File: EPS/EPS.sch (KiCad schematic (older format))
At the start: 2 parts, among them J6 CAN

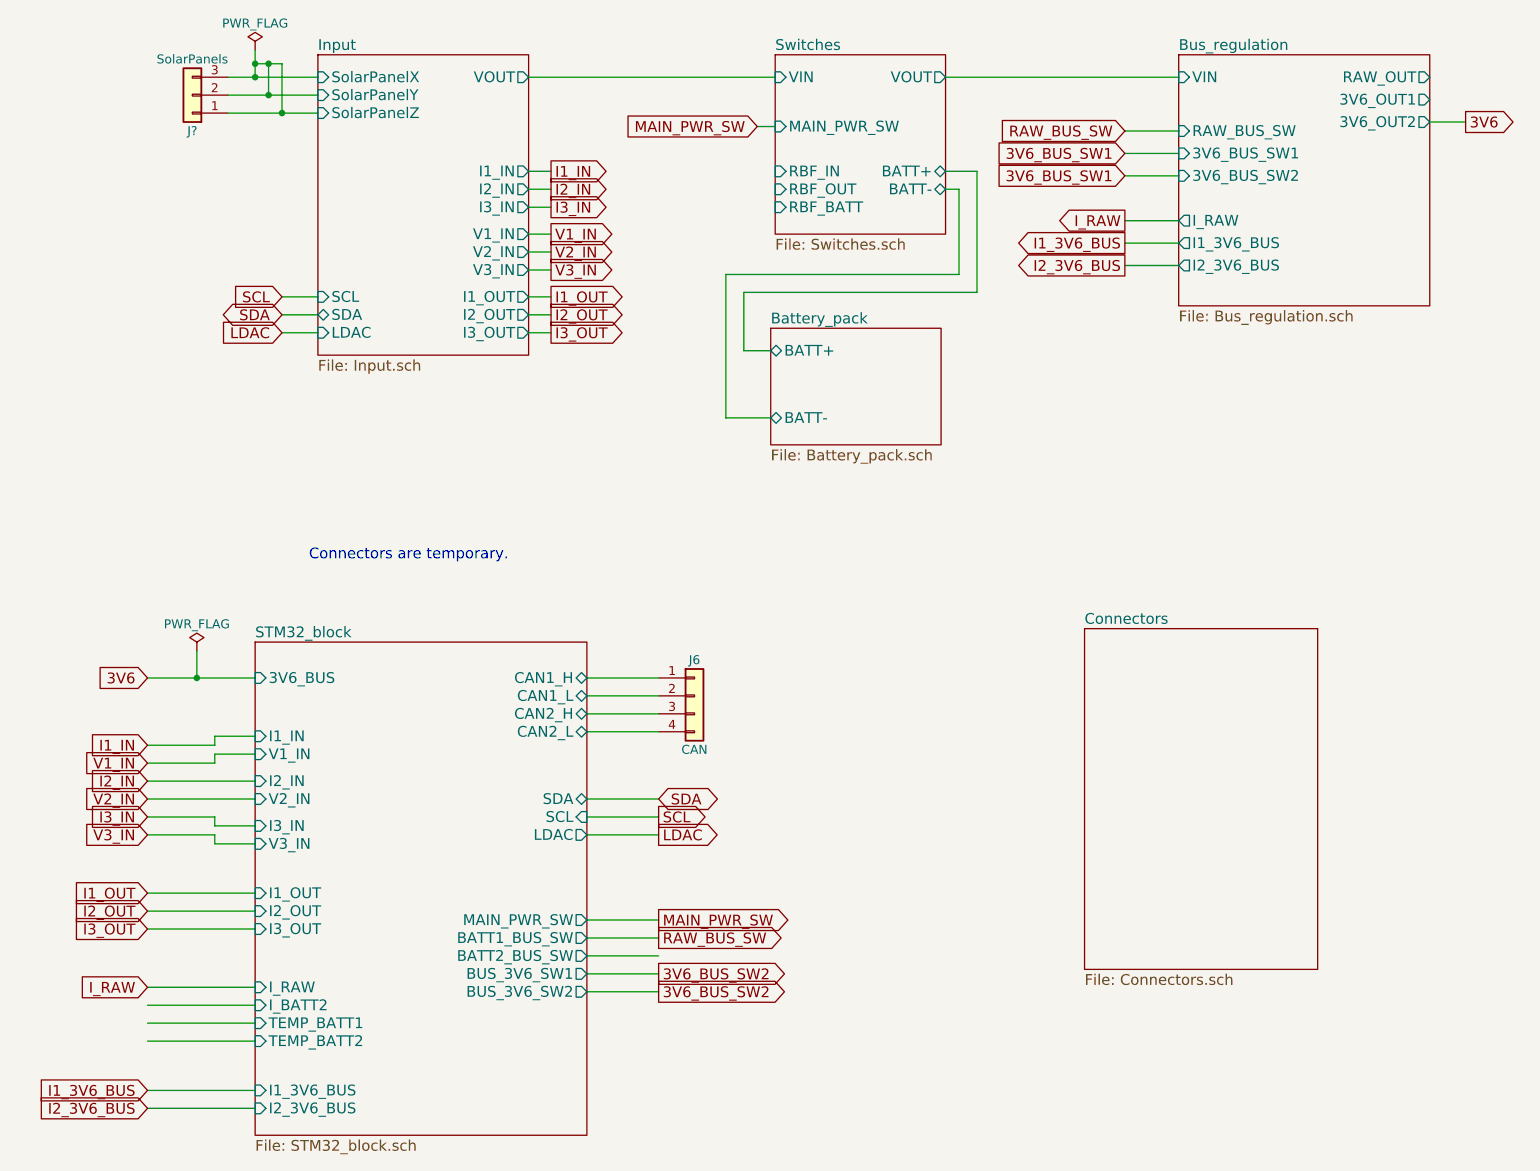
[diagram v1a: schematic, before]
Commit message: Updated Schematics
Added:
- digital pot
- digital loads
- updated  switch sheet to block two ways before battery
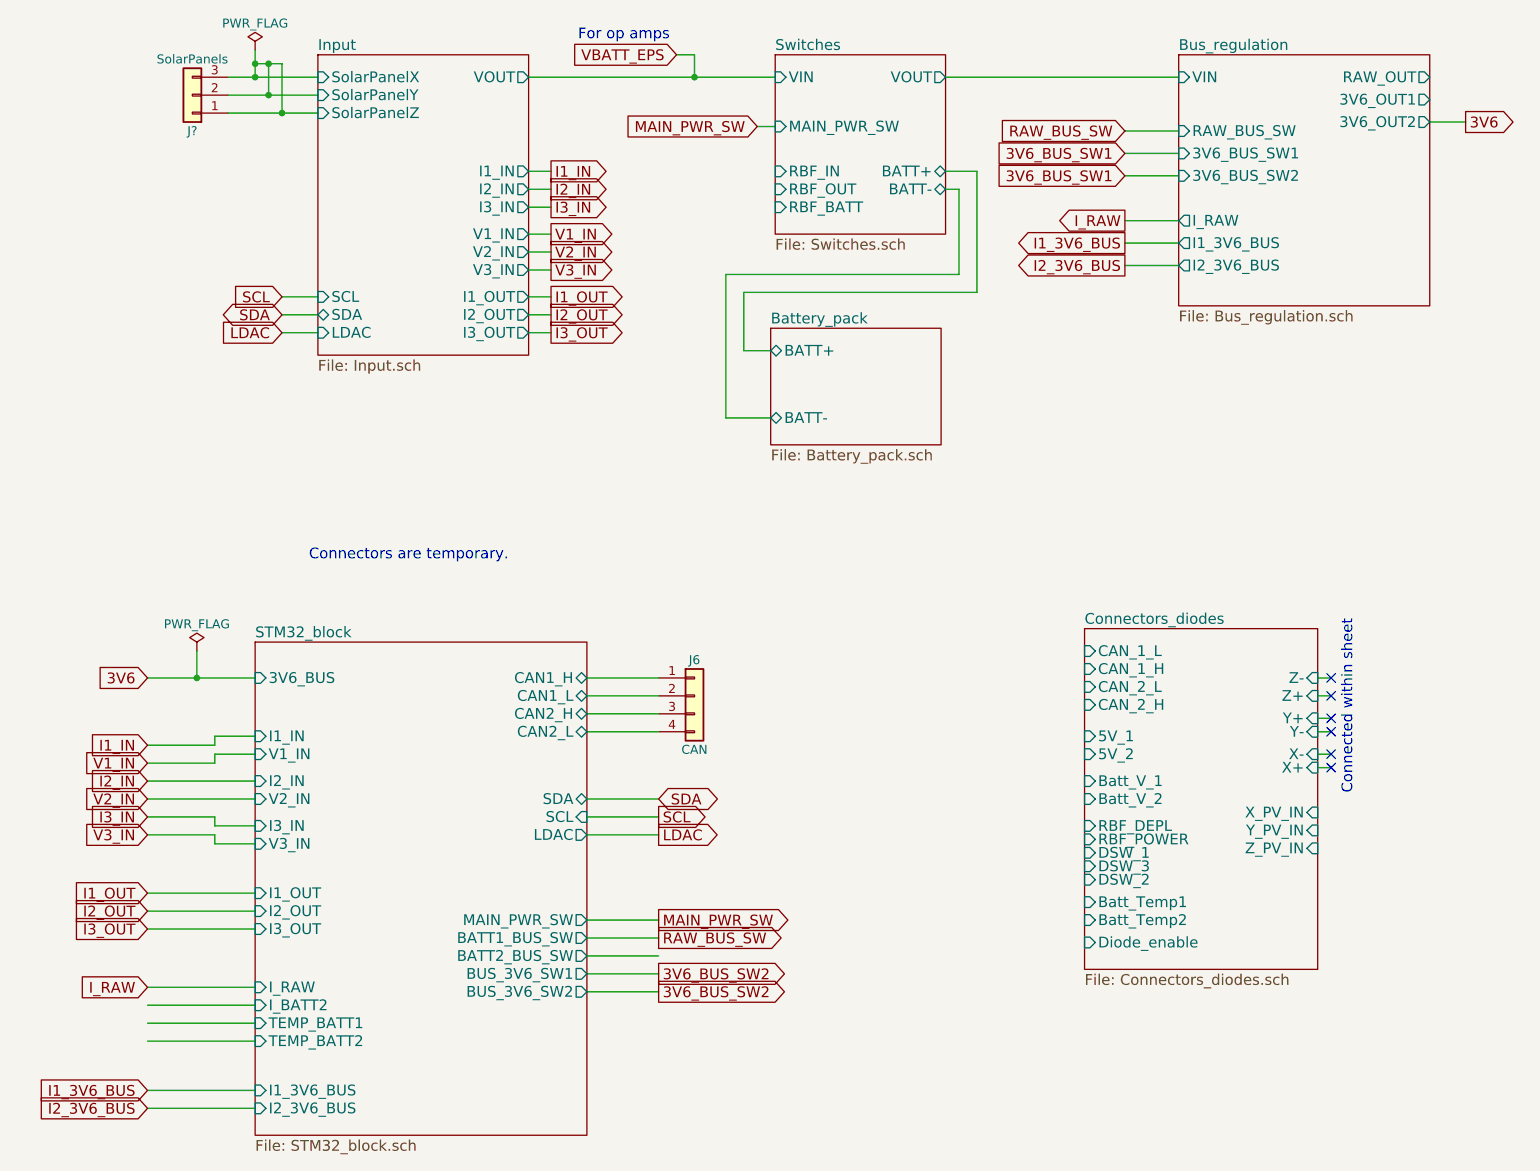
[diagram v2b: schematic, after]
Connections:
- net labels added: VBATT_EPS
- wire segments 76 -> 84
- no-connect marks 0 -> 6
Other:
- note added: "Connected within sheet\n"
- note added: "For op amps"
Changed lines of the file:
@@
 LIBS:tps7a7002
 LIBS:max5395
+LIBS:ina210
+LIBS:ncs20071
 LIBS:EPS-cache
 EELAYER 25 0
@@
 $Descr A4 11693 8268
 encoding utf-8
-Sheet 1 13
+Sheet 1 14
 Title "EPS"
 Date "2018-02-16"
@@
 S 7550 4175 1300 1900
 U 5A810768
-F0 "Connectors" 60
-F1 "Connectors.sch" 60
+F0 "Connectors_diodes" 60
+F1 "Connectors_diodes.sch" 60
+F2 "CAN_1_L" I L 7550 4300 60
+F3 "CAN_1_H" I L 7550 4400 60
+F4 "CAN_2_L" I L 7550 4500 60
+F5 "CAN_2_H" I L 7550 4600 60
+F6 "5V_1" I L 7550 4775 60
+F7 "5V_2" I L 7550 4875 60
+F8 "Batt_V_1" I L 7550 5025 60
+F9 "Batt_V_2" I L 7550 5125 60
+F10 "RBF_DEPL" I L 7550 5275 60
+F11 "RBF_POWER" I L 7550 5350 60
+F12 "DSW_1" I L 7550 5425 60
+F13 "DSW_3" I L 7550 5500 60
+F14 "DSW_2" I L 7550 5575 60
+F15 "X-" I R 8850 4875 60
+F16 "Z-" I R 8850 4450 60
+F17 "Z+" I R 8850 4550 60
+F18 "Y-" I R 8850 4750 60
+F19 "Y+" I R 8850 4675 60
+F20 "X+" I R 8850 4950 60
+F21 "Batt_Temp1" I L 7550 5700 60
+F22 "Batt_Temp2" I L 7550 5800 60
+F23 "Diode_enable" I L 7550 5925 60
+F24 "X_PV_IN" I R 8850 5200 60
+F25 "Y_PV_IN" I R 8850 5300 60
+F26 "Z_PV_IN" I R 8850 5400 60
 $EndSheet
 $Comp
@@
 Text GLabel 2325 4450 0    60   Input ~ 0
 3V6
+Wire Wire Line
+	8850 4450 8925 4450
+Wire Wire Line
+	8850 4550 8925 4550
+Wire Wire Line
+	8850 4675 8925 4675
+Wire Wire Line
+	8850 4750 8925 4750
+Wire Wire Line
+	8850 4875 8925 4875
+Wire Wire Line
+	8850 4950 8925 4950
+NoConn ~ 8925 4950
+NoConn ~ 8925 4875
+NoConn ~ 8925 4750
+NoConn ~ 8925 4675
+NoConn ~ 8925 4550
+NoConn ~ 8925 4450
+Text Notes 9050 4125 3    60   ~ 0
+Connected within sheet\n
+Text GLabel 5275 975  0    60   Input ~ 0
+VBATT_EPS
+Wire Wire Line
+	5275 975  5375 975
+Wire Wire Line
+	5375 975  5375 1100
+Connection ~ 5375 1100
+Text Notes 4725 900  0    60   ~ 0
+For op amps
 $EndSCHEMATC

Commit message: Add files via upload
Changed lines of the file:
@@
 F2 "BATT-" B L 5800 3000 60
 F3 "BATT+" B L 5800 2625 60
+F4 "BATT_HEATER" I L 5800 2750 60
+F5 "BATT_CELL1_VOLTAGE" O L 5800 2850 60
+F6 "BATT_CELL2_VOLTAGE" O L 5800 2925 60
 $EndSheet
 Wire Wire Line
